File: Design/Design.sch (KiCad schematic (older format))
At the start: 25 parts, among them Q1 IRF840, U2 LM393, U3 LM7805

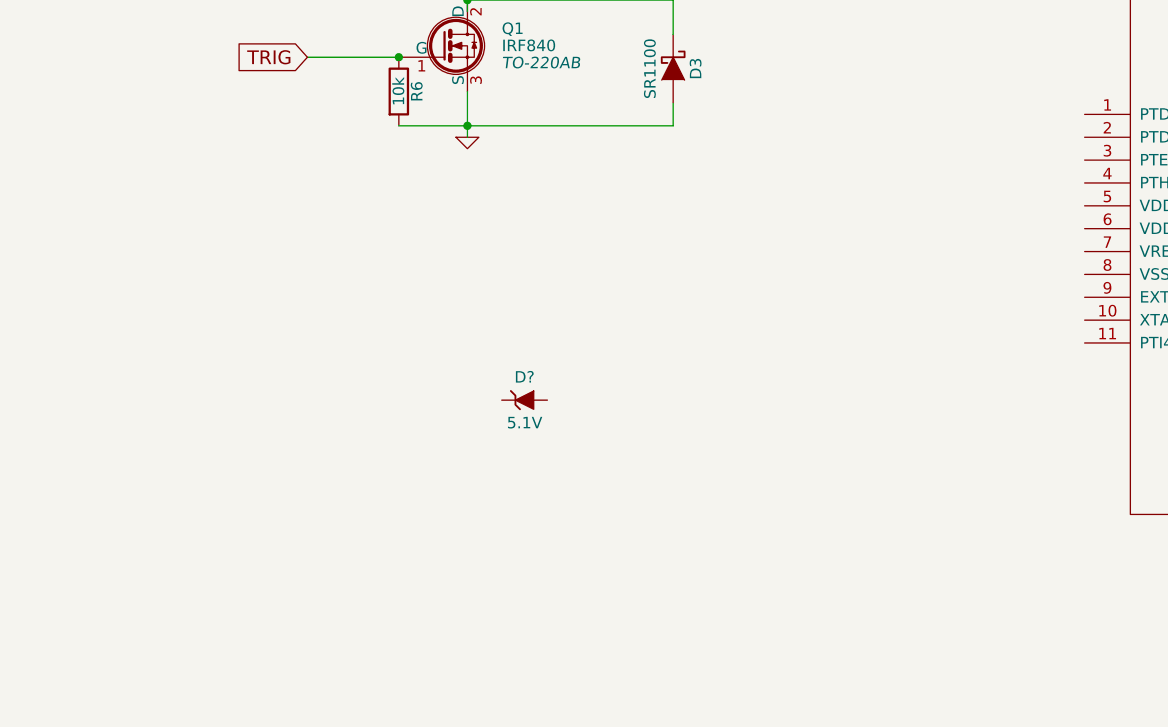
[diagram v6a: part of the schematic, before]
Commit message: Updated the design with the new VRS conditioning circuit
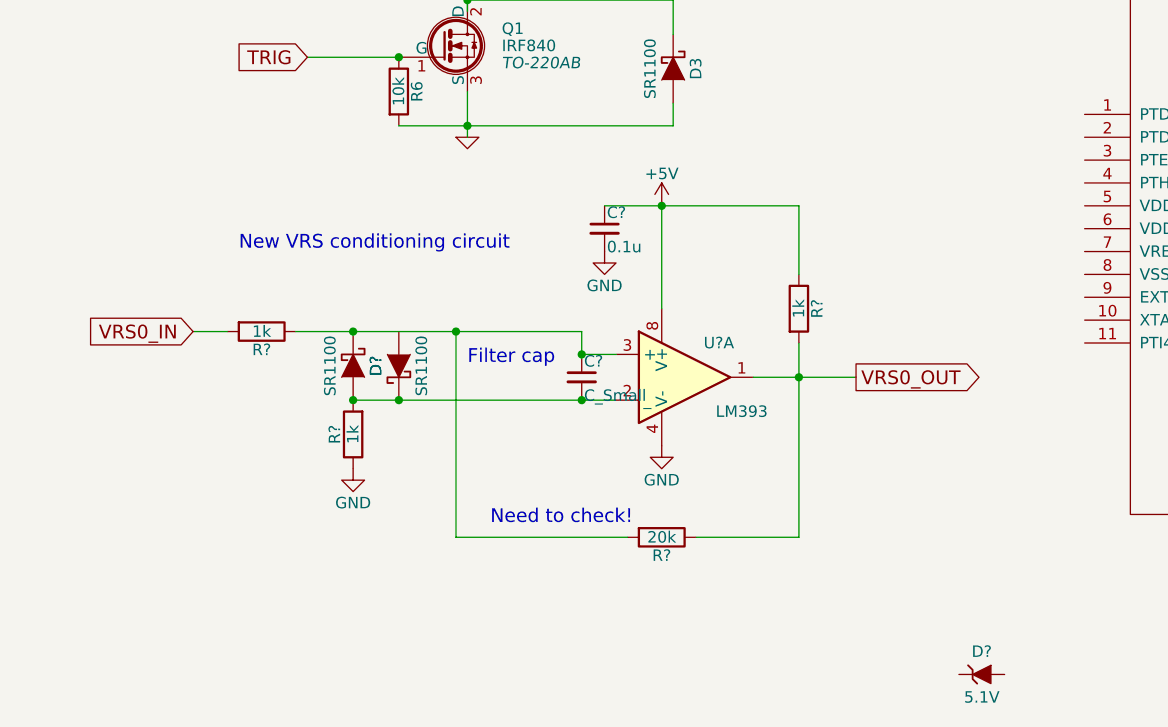
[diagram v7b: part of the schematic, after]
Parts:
- added C?: 0.1u, symbol C_Small
- added C?: C_Small, symbol C_Small
- added D? (x2): SR1100, symbol SR1100
- added R? (x3): 1k, symbol R
- added R?: 20k, symbol R
- added U?: LM393, symbol LM393
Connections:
- net +5V: now also C?.1, R?.1, U?.8 (V+)
- net GND: now also C?.2, R?.1, U?.4 (V-)
- net VRS0_OUT: now also R?.1, R?.2, U?.1
- new net: C?.2, D?.1 (K), D?.2 (A), R?.2, U?.2 (_)
- new net: C?.1, D?.1 (K), R?.1, R?.2, U?.3 (+)
- new net VRS0_IN: R?.2
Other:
- note added: "Filter cap"
- note added: "Need to check!"
- note added: "New VRS conditioning circuit"
- moved on the sheet: D?
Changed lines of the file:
@@
 	1    0    0    -1
 $EndComp
-Wire Wire Line
-	2500 4050 2500 4250
 $Comp
 L R R6
@@
 	1    0    0    -1
 $EndComp
-Wire Wire Line
-	2200 4200 3400 4200
-Connection ~ 2500 4200
 $Comp
 L SR1100 D3
@@
 	0    1    1    0
 $EndComp
-Wire Wire Line
-	3400 4200 3400 4100
-Wire Wire Line
-	3400 3650 3400 3800
-Wire Wire Line
-	2500 3600 2500 3700
-Connection ~ 2500 3650
 Text Notes 2750 3000 0    60   ~ 0
 Coil / injector driver
 Text GLabel 1800 3900 0    60   Input ~ 0
 TRIG
-Wire Wire Line
-	2200 3900 1800 3900
-Connection ~ 2200 3900
-Wire Wire Line
-	3400 3650 2500 3650
 $Comp
 L LM7805 U3
@@
 	1    0    0    -1
 $EndComp
-Wire Wire Line
-	6550 1400 6550 1500
-Wire Wire Line
-	6200 1500 7350 1500
-Wire Wire Line
-	6950 1400 6950 1600
-Connection ~ 6950 1500
 $Comp
 L C_Small C2
@@
 	1    0    0    -1
 $EndComp
-Wire Wire Line
-	7350 1050 7350 1200
-Wire Wire Line
-	7350 1500 7350 1400
-Connection ~ 7350 1100
 $Comp
 L RVAR R8
@@
 	1    0    0    -1
 $EndComp
-Wire Wire Line
-	8900 1950 8900 2100
 $Comp
 L GND-RESCUE-Design #PWR05
@@
 Text GLabel 9150 2050 2    60   Output ~ 0
 IAT_OUT
-Wire Wire Line
-	9150 2050 8900 2050
-Connection ~ 8900 2050
 Text Notes 8450 1500 0    60   ~ 0
 Intake temperature sensor\nvoltage divider
@@
 	1    0    0    -1
 $EndComp
-Connection ~ 900  1100
 Text GLabel 1100 1100 2    60   Output ~ 0
 VRS_TH
-Wire Wire Line
-	1100 1100 900  1100
 $Comp
 L GND-RESCUE-Design #PWR06
@@
 	0    1    1    0
 $EndComp
-Connection ~ 3000 1250
 $Comp
 L GND-RESCUE-Design #PWR07
@@
 Text GLabel 1200 1800 0    60   Input ~ 0
 VRS0_LOW
-Wire Wire Line
-	1200 1650 1500 1650
-Wire Wire Line
-	1500 1650 1500 1850
-Wire Wire Line
-	1500 1800 1200 1800
 $Comp
 L GND-RESCUE-Design #PWR09
@@
 	1    0    0    -1
 $EndComp
-Connection ~ 1500 1800
 Text GLabel 2800 1250 0    60   Input ~ 0
 VRS0_HIGH
-Wire Wire Line
-	2800 1250 3750 1250
 $Comp
 L GND-RESCUE-Design #PWR010
@@
 	1    0    0    -1
 $EndComp
-Wire Wire Line
-	3950 1050 3950 950
-Wire Wire Line
-	3950 950  4350 950
-Wire Wire Line
-	4350 950  4350 1050
-Connection ~ 3950 950
 $Comp
 L SR1100 D4
@@
 	0    1    1    0
 $EndComp
-Connection ~ 3000 2200
 $Comp
 L GND-RESCUE-Design #PWR012
@@
 Text GLabel 2800 2200 0    60   Input ~ 0
 VRS1_HIGH
-Wire Wire Line
-	2800 2200 3750 2200
 $Comp
 L GND-RESCUE-Design #PWR014
@@
 	1    0    0    -1
 $EndComp
-Wire Wire Line
-	3950 2000 3950 1900
-Wire Wire Line
-	3950 1900 4350 1900
-Wire Wire Line
-	4350 1900 4350 2000
-Connection ~ 3950 1900
 $Comp
 L +BATT #PWR016
@@
 Text GLabel 4550 1350 2    60   Output ~ 0
 VRS0_OUT
-Wire Wire Line
-	4550 1350 4350 1350
-Connection ~ 4350 1350
 Text GLabel 4600 2300 2    60   Output ~ 0
 VRS1_OUT
-Wire Wire Line
-	4350 2300 4600 2300
-Connection ~ 4350 2300
 $Comp
 L +BATT #PWR017
@@
 Text GLabel 6450 2200 0    60   Input ~ 0
 VRS_OUT
-Connection ~ 6750 2200
 $Comp
 L +5V #PWR?
@@
 L ZENERsmall D?
 U 1 1 5718A5FC
-P 2750 5400
-F 0 "D?" H 2750 5500 50  0000 C CNN
-F 1 "5.1V" H 2750 5300 50  0000 C CNN
-F 2 "" H 2750 5400 50  0000 C CNN
-F 3 "" H 2750 5400 50  0000 C CNN
-	1    2750 5400
+P 4750 6600
+F 0 "D?" H 4750 6700 50  0000 C CNN
+F 1 "5.1V" H 4750 6500 50  0000 C CNN
+F 2 "" H 4750 6600 50  0000 C CNN
+F 3 "" H 4750 6600 50  0000 C CNN
+	1    4750 6600
 	1    0    0    -1
 $EndComp
@@
 	0    1    1    0
 $EndComp
+$Comp
+L LM393 U?
+U 1 1 571EEE41
+P 3450 5300
+F 0 "U?" H 3600 5450 50  0000 C CNN
+F 1 "LM393" H 3700 5150 50  0000 C CNN
+F 2 "" H 3450 5300 50  0000 C CNN
+F 3 "" H 3450 5300 50  0000 C CNN
+	1    3450 5300
+	1    0    0    -1
+$EndComp
+$Comp
+L +5V #PWR?
+U 1 1 571EEF43
+P 3350 4550
+F 0 "#PWR?" H 3350 4400 50  0001 C CNN
+F 1 "+5V" H 3350 4690 50  0000 C CNN
+F 2 "" H 3350 4550 50  0000 C CNN
+F 3 "" H 3350 4550 50  0000 C CNN
+	1    3350 4550
+	1    0    0    -1
+$EndComp
+$Comp
+L GND #PWR?
+U 1 1 571EEFA8
+P 3350 5600
+F 0 "#PWR?" H 3350 5350 50  0001 C CNN
+F 1 "GND" H 3350 5450 50  0000 C CNN
+F 2 "" H 3350 5600 50  0000 C CNN
+F 3 "" H 3350 5600 50  0000 C CNN
+	1    3350 5600
+	1    0    0    -1
+$EndComp
+$Comp
+L GND #PWR?
+U 1 1 571EF00D
+P 3100 4750
+F 0 "#PWR?" H 3100 4500 50  0001 C CNN
+F 1 "GND" H 3100 4600 50  0000 C CNN
+F 2 "" H 3100 4750 50  0000 C CNN
+F 3 "" H 3100 4750 50  0000 C CNN
+	1    3100 4750
+	1    0    0    -1
+$EndComp
+$Comp
+L C_Small C?
+U 1 1 571EF1D1
+P 3100 4650
+F 0 "C?" H 3110 4720 50  0000 L CNN
+F 1 "0.1u" H 3110 4570 50  0000 L CNN
+F 2 "" H 3100 4650 50  0000 C CNN
+F 3 "" H 3100 4650 50  0000 C CNN
+	1    3100 4650
+	1    0    0    -1
+$EndComp
+$Comp
+L R R?
+U 1 1 571EF7E4
+P 1600 5100
+F 0 "R?" V 1680 5100 50  0000 C CNN
+F 1 "1k" V 1600 5100 50  0000 C CNN
+F 2 "" V 1530 5100 50  0000 C CNN
+F 3 "" H 1600 5100 50  0000 C CNN
+	1    1600 5100
+	0    1    1    0
+$EndComp
+$Comp
+L R R?
+U 1 1 571EF910
+P 2000 5550
+F 0 "R?" V 2080 5550 50  0000 C CNN
+F 1 "1k" V 2000 5550 50  0000 C CNN
+F 2 "" V 1930 5550 50  0000 C CNN
+F 3 "" H 2000 5550 50  0000 C CNN
+	1    2000 5550
+	-1   0    0    1
+$EndComp
+$Comp
+L SR1100 D?
+U 1 1 571F01EB
+P 2000 5250
+F 0 "D?" H 2000 5350 50  0000 C CNN
+F 1 "SR1100" H 2000 5150 50  0000 C CNN
+F 2 "" H 2000 5250 50  0000 C CNN
+F 3 "" H 2000 5250 50  0000 C CNN
+	1    2000 5250
+	0    1    1    0
+$EndComp
+$Comp
+L SR1100 D?
+U 1 1 571F0279
+P 2200 5250
+F 0 "D?" H 2200 5350 50  0000 C CNN
+F 1 "SR1100" H 2200 5150 50  0000 C CNN
+F 2 "" H 2200 5250 50  0000 C CNN
+F 3 "" H 2200 5250 50  0000 C CNN
+	1    2200 5250
+	0    -1   -1   0
+$EndComp
+Text GLabel 1300 5100 0    60   Input ~ 0
+VRS0_IN
+$Comp
+L GND #PWR?
+U 1 1 571F0666
+P 2000 5700
+F 0 "#PWR?" H 2000 5450 50  0001 C CNN
+F 1 "GND" H 2000 5550 50  0000 C CNN
+F 2 "" H 2000 5700 50  0000 C CNN
+F 3 "" H 2000 5700 50  0000 C CNN
+	1    2000 5700
+	1    0    0    -1
+$EndComp
+$Comp
+L C_Small C?
+U 1 1 571F0984
+P 3000 5300
+F 0 "C?" H 3010 5370 50  0000 L CNN
+F 1 "C_Small" H 3010 5220 50  0000 L CNN
+F 2 "" H 3000 5300 50  0000 C CNN
+F 3 "" H 3000 5300 50  0000 C CNN
+	1    3000 5300
+	1    0    0    -1
+$EndComp
+Wire Wire Line
+	2500 4050 2500 4250
+Wire Wire Line
+	2200 4200 3400 4200
+Connection ~ 2500 4200
+Wire Wire Line
+	3400 4200 3400 4100
+Wire Wire Line
+	3400 3650 3400 3800
+Wire Wire Line
+	2500 3600 2500 3700
+Connection ~ 2500 3650
+Wire Wire Line
+	2200 3900 1800 3900
+Connection ~ 2200 3900
+Wire Wire Line
+	3400 3650 2500 3650
+Wire Wire Line
+	6550 1400 6550 1500
+Wire Wire Line
+	6200 1500 7350 1500
+Wire Wire Line
+	6950 1400 6950 1600
+Connection ~ 6950 1500
+Wire Wire Line
+	7350 1050 7350 1200
+Wire Wire Line
+	7350 1500 7350 1400
+Connection ~ 7350 1100
+Wire Wire Line
+	8900 1950 8900 2100
+Wire Wire Line
+	9150 2050 8900 2050
+Connection ~ 8900 2050
+Connection ~ 900  1100
+Wire Wire Line
+	1100 1100 900  1100
+Connection ~ 3000 1250
+Wire Wire Line
+	1200 1650 1500 1650
+Wire Wire Line
+	1500 1650 1500 1850
+Wire Wire Line
+	1500 1800 1200 1800
+Connection ~ 1500 1800
+Wire Wire Line
+	2800 1250 3750 1250
+Wire Wire Line
+	3950 1050 3950 950
+Wire Wire Line
+	3950 950  4350 950
+Wire Wire Line
+	4350 950  4350 1050
+Connection ~ 3950 950
+Connection ~ 3000 2200
+Wire Wire Line
+	2800 2200 3750 2200
+Wire Wire Line
+	3950 2000 3950 1900
+Wire Wire Line
+	3950 1900 4350 1900
+Wire Wire Line
+	4350 1900 4350 2000
+Connection ~ 3950 1900
+Wire Wire Line
+	4550 1350 4350 1350
+Connection ~ 4350 1350
+Wire Wire Line
+	4350 2300 4600 2300
+Connection ~ 4350 2300
+Connection ~ 6750 2200
 Wire Wire Line
 	6200 1500 6200 1300
@@
 Connection ~ 6550 1100
 Connection ~ 6200 1100
+Wire Wire Line
+	3350 4550 3350 5000
+Connection ~ 3350 4550
+Wire Wire Line
+	1750 5100 3000 5100
+Connection ~ 2000 5400
+Connection ~ 2000 5100
+Wire Wire Line
+	3000 5200 3150 5200
+Wire Wire Line
+	3100 4550 3950 4550
+$Comp
+L R R?
+U 1 1 571F173D
+P 3950 5000
+F 0 "R?" V 4030 5000 50  0000 C CNN
+F 1 "1k" V 3950 5000 50  0000 C CNN
+F 2 "" V 3880 5000 50  0000 C CNN
+F 3 "" H 3950 5000 50  0000 C CNN
+	1    3950 5000
+	1    0    0    -1
+$EndComp
+Wire Wire Line
+	3950 4550 3950 4850
+Wire Wire Line
+	3950 5150 3950 6000
+Wire Wire Line
+	3750 5300 4200 5300
+Text Notes 2500 5250 0    60   ~ 0
+Filter cap
+$Comp
+L R R?
+U 1 1 571F1CD6
+P 3350 6000
+F 0 "R?" V 3430 6000 50  0000 C CNN
+F 1 "20k" V 3350 6000 50  0000 C CNN
+F 2 "" V 3280 6000 50  0000 C CNN
+F 3 "" H 3350 6000 50  0000 C CNN
+	1    3350 6000
+	0    1    1    0
+$EndComp
+Wire Wire Line
+	2450 6000 3200 6000
+Wire Wire Line
+	3950 6000 3500 6000
+Connection ~ 3950 5300
+Wire Wire Line
+	1450 5100 1300 5100
+Text GLabel 4200 5300 2    60   Output ~ 0
+VRS0_OUT
+Wire Wire Line
+	3000 5100 3000 5200
+Text Notes 2600 5950 0    60   ~ 0
+Need to check!
+Text Notes 1500 4750 0    60   ~ 0
+New VRS conditioning circuit
+Wire Wire Line
+	2450 5100 2450 6000
+Connection ~ 2450 5100
+Wire Wire Line
+	3150 5400 2000 5400
+Connection ~ 3000 5400
+Connection ~ 2200 5400
+Connection ~ 3000 5200
 $EndSCHEMATC
